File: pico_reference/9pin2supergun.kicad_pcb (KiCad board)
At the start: 2 copper layers, 61 x 52.5 mm, 11 parts, among them J1 Controller Input, J2 Output, SW1 SW_Wuerth_450301014042, SW2 SW_Push, U1 SN74AVC4T245PW, U2 SN74LVC8T245

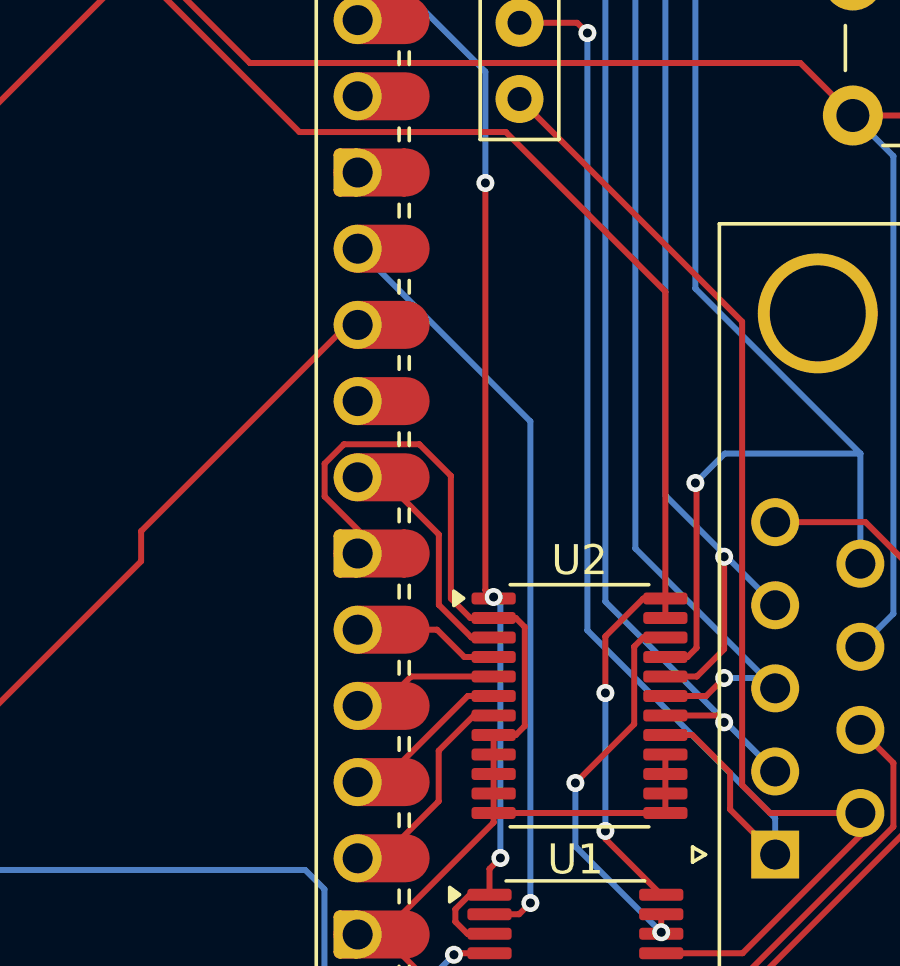
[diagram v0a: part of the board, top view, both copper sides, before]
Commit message: Missed out the track from /OE to the actual chips that use it, which is unhelpful.
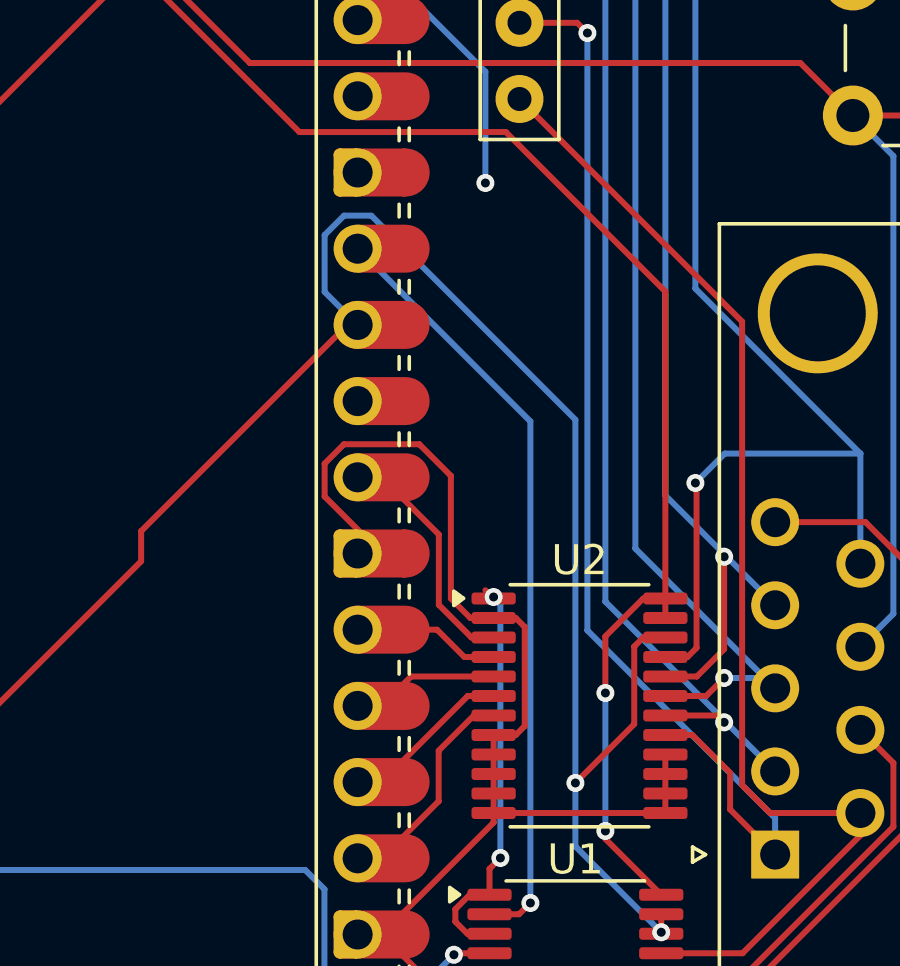
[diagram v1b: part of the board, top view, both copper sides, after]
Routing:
- net /~{OE}: track 93.8 -> 120.8 mm
- net +3.3V: track 98.7 -> 85.1 mm
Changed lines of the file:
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@@
-	)
-	(segment
-		(start 129 114.575)
-		(end 129 101)
-		(width 0.2)
-		(layer "F.Cu")
-		(net 12)
 	)
 	(segment
@@
 	)
 	(segment
+		(start 132 108.89045)
+		(end 132 121)
+		(width 0.2)
+		(layer "B.Cu")
+		(net 23)
+	)
+	(segment
 		(start 132 121)
 		(end 132 123.1125)
 		(width 0.2)
 		(layer "B.Cu")
+		(net 23)
+	)
+	(segment
+		(start 124.28645 102.089)
+		(end 125.19855 102.089)
+		(width 0.2)
+		(layer "B.Cu")
+		(net 23)
+	)
+	(segment
+		(start 124.7425 105.73)
+		(end 123.6415 104.629)
+		(width 0.2)
+		(layer "B.Cu")
+		(net 23)
+	)
+	(segment
+		(start 123.6415 104.629)
+		(end 123.6415 102.73395)
+		(width 0.2)
+		(layer "B.Cu")
+		(net 23)
+	)
+	(segment
+		(start 123.6415 102.73395)
+		(end 124.28645 102.089)
+		(width 0.2)
+		(layer "B.Cu")
+		(net 23)
+	)
+	(segment
+		(start 125.19855 102.089)
+		(end 132 108.89045)
+		(width 0.2)
+		(layer "B.Cu")

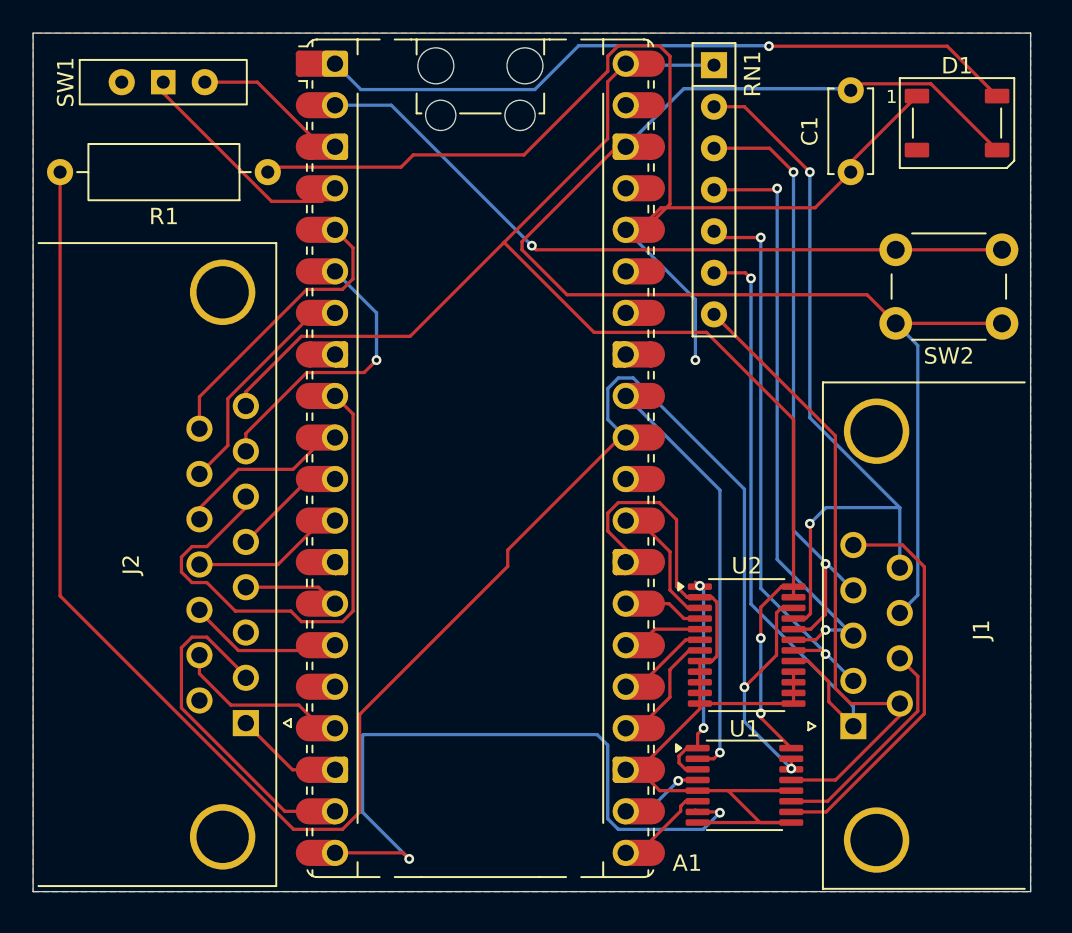
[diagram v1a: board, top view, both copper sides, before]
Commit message: And somehow the 3.3v also got disconnected there?
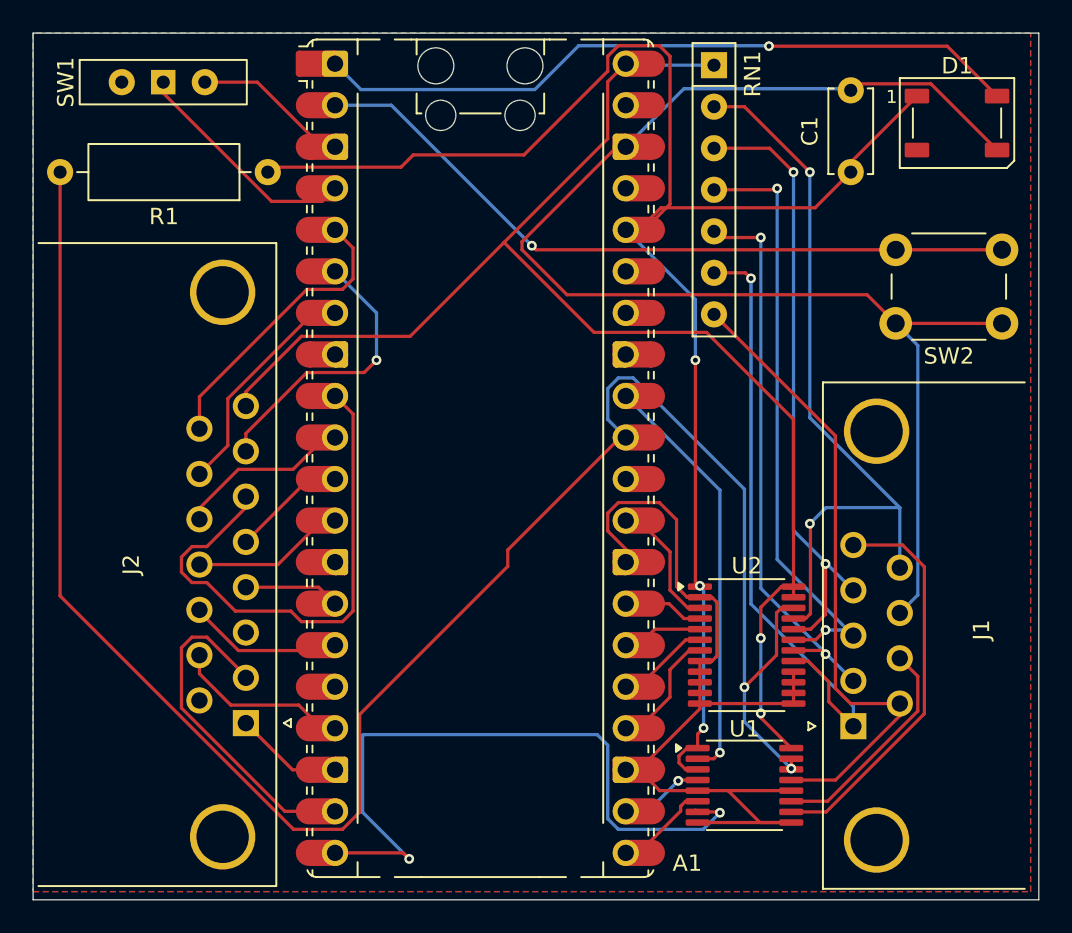
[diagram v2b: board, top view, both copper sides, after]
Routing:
- net +3.3V: track 85.1 -> 98.7 mm
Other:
- board size 61 x 52.5 mm -> 61.5 x 53 mm
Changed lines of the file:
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@@
 	(gr_rect
 		(start 88.5 81)
-		(end 149.5 133.5)
+		(end 150 134)
 		(stroke
 			(width 0.05)
@@
 	)
 	(segment
-		(start 129.275 114.85)
-		(end 129 114.575)
-		(width 0.2)
-		(layer "F.Cu")
-		(net 12)
-	)
-	(segment
 		(start 128.48013 124.725)
 		(end 128 125.20513)
@@
 	)
 	(segment
+		(start 129 101)
+		(end 129 114.575)
+		(width 0.2)
+		(layer "F.Cu")
+		(net 12)
+	)
+	(segment
 		(start 136.319 91.681)
 		(end 126.8915 91.681)
 		(width 0.2)
 		(layer "F.Cu")
+		(net 12)
+	)
+	(segment
+		(start 129 114.575)
+		(end 129.275 114.85)
+		(width 0.2)
+		(layer "F.Cu")

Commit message: And the DRC didn't tell me that coin wasn't connected either
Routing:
- net /Coin: track 0.00 -> 6.83 mm
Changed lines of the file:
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@@
+	)
+	(segment
+		(start 104.825331 120.97)
+		(end 101.510331 117.655)
+		(width 0.2)
+		(layer "B.Cu")
+		(net 24)
+	)
+	(segment
+		(start 106.9625 120.97)
+		(end 104.825331 120.97)
+		(width 0.2)
+		(layer "B.Cu")
+		(net 24)
 	)
 	(segment

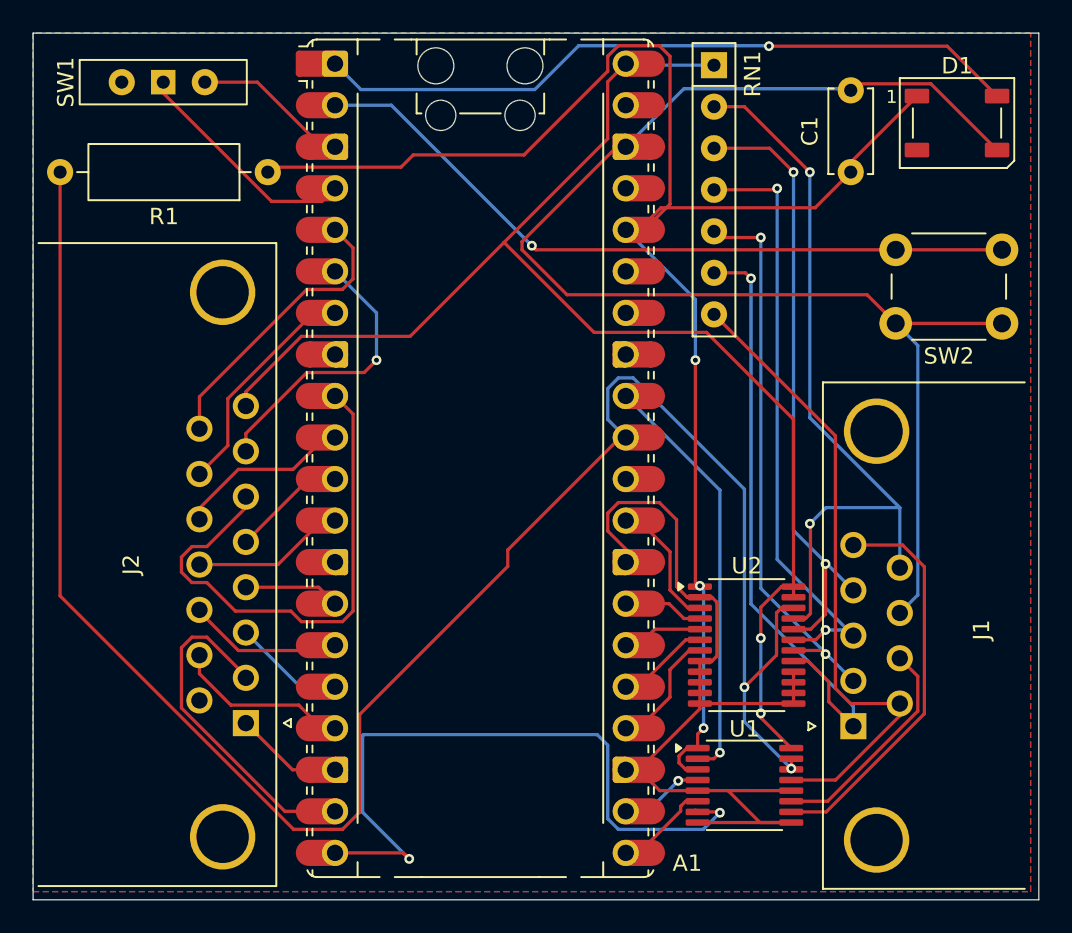
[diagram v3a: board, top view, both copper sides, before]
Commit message: Update Pico reference design to use different level shifters
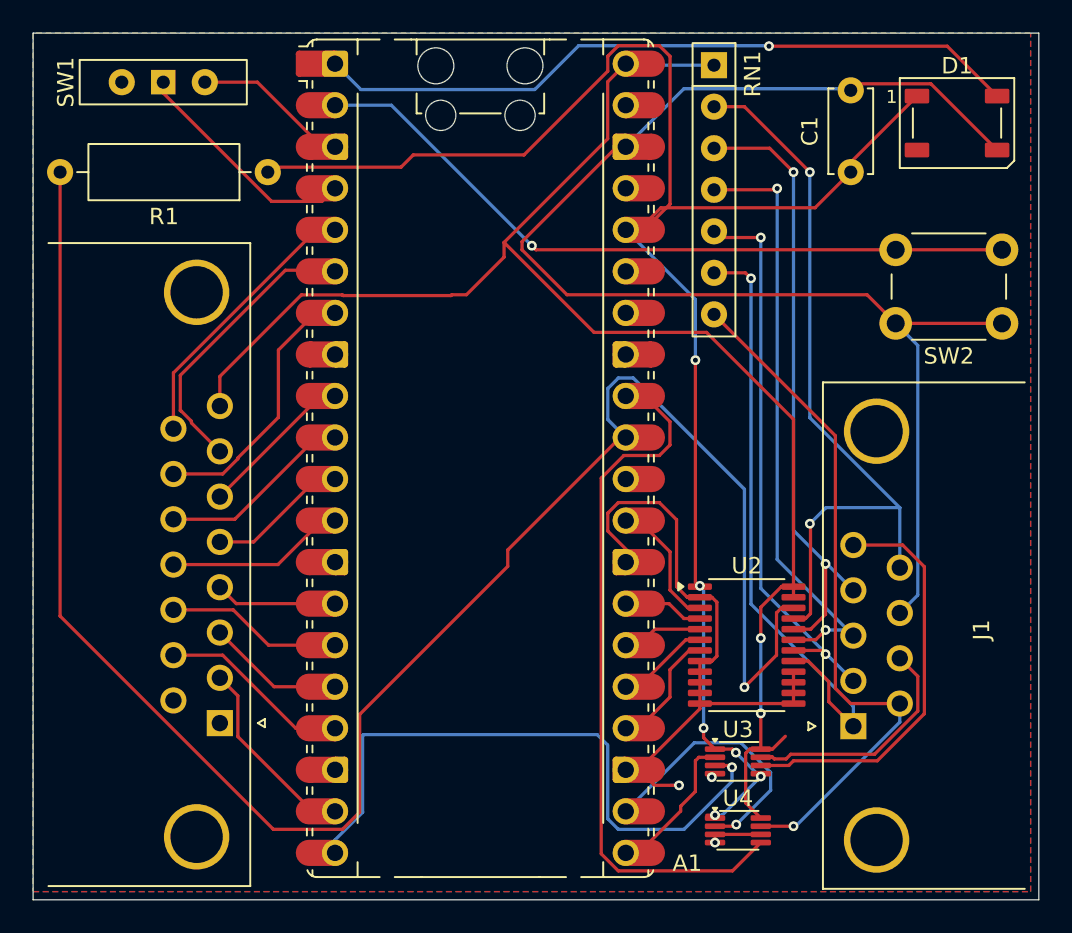
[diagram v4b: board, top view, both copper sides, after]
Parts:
- removed U1: SN74AVC4T245PW, Package_SO:TSSOP-16_4.4x5mm_P0.65mm
- added U3: SN74LVC2T45DCUR, Package_SO:VSSOP-8_2.3x2mm_P0.5mm, F.Cu at (131.6, 125.5)
- added U4: SN74LVC2T45DCUR, Package_SO:VSSOP-8_2.3x2mm_P0.5mm, F.Cu at (131.6, 129.8)
- J2: footprint Connector_Dsub:DSUB-15_Socket_Horizontal_P2.77x2.84mm_EdgePinOffset9.90mm_Housed_MountingHolesOffset11.32mm -> Connector_Dsub:DSUB-15_Socket_Horizontal_P2.77x2.84mm_EdgePinOffset7.70mm_Housed_MountingHolesOffset9.12mm
- moved J2 1.59 mm to (99.9, 123.2)
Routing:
- net /Right: track 32.4 -> 9.59 mm
- net GND: track 157.7 -> 137.5 mm, vias 0 -> 3
- net /Pin 6 Direction: track 25.7 -> 43.7 mm, vias 1 -> 0
- net /3.3V Fire1: track 5.19 -> 16.7 mm
- net VBUS: track 84.9 -> 94.1 mm
- net /Button 6: track 21.0 -> 11.9 mm
- net /~{OE}: track 120.8 -> 114.7 mm, vias 2 -> 1
- net +3.3V: track 98.7 -> 103.6 mm, vias 3 -> 6
- net /3.3V Latch/Power: track 42.3 -> 38.7 mm, vias 2 -> 1
- net /3.3V Power/Select: track 5.08 -> 8.35 mm
- net /5V Fire1: track 39.3 -> 42.5 mm, vias 0 -> 1
- net /Button 2: track 7.04 -> 10.2 mm
- net /Left: track 14.1 -> 16.9 mm
- net /Button 3: track 8.61 -> 10.2 mm
- net /Coin: track 6.83 -> 8.42 mm
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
